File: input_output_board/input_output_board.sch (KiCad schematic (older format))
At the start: 18 parts, among them J1 Neutrik_NCJ6FA-H, J2 Neutrik_NCJ6FA-H, J3 Neutrik_NCJ6FA-H, J4 Neutrik_NCJ6FA-H, J5 AudioJack3, J6 Conn_02x05_Odd_Even, J7 Molex_SL_01x02_Male, J8 Molex_SL_01x02_Male, K1 G6S-2, K2 G6S-2, K3 G6S-2, K4 G6S-2, K5 G6S-2

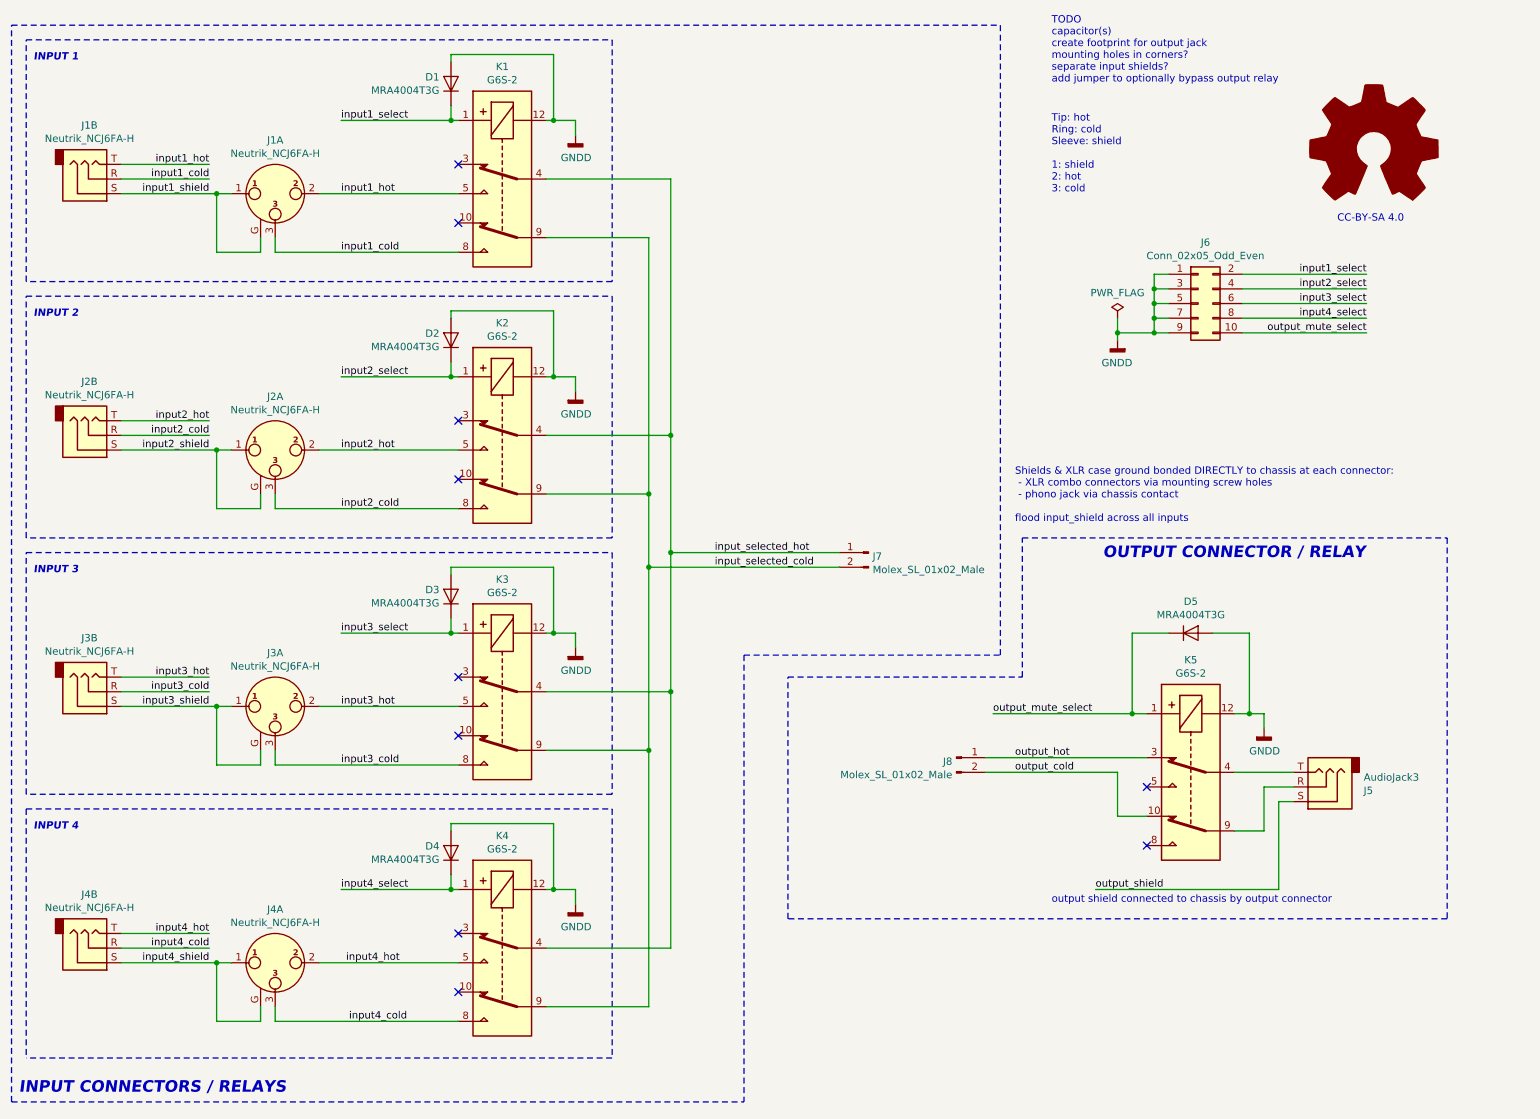
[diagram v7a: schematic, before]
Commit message: add jumpers to schematic to optionally bypass output relay. Update TODO. Clean up schematic
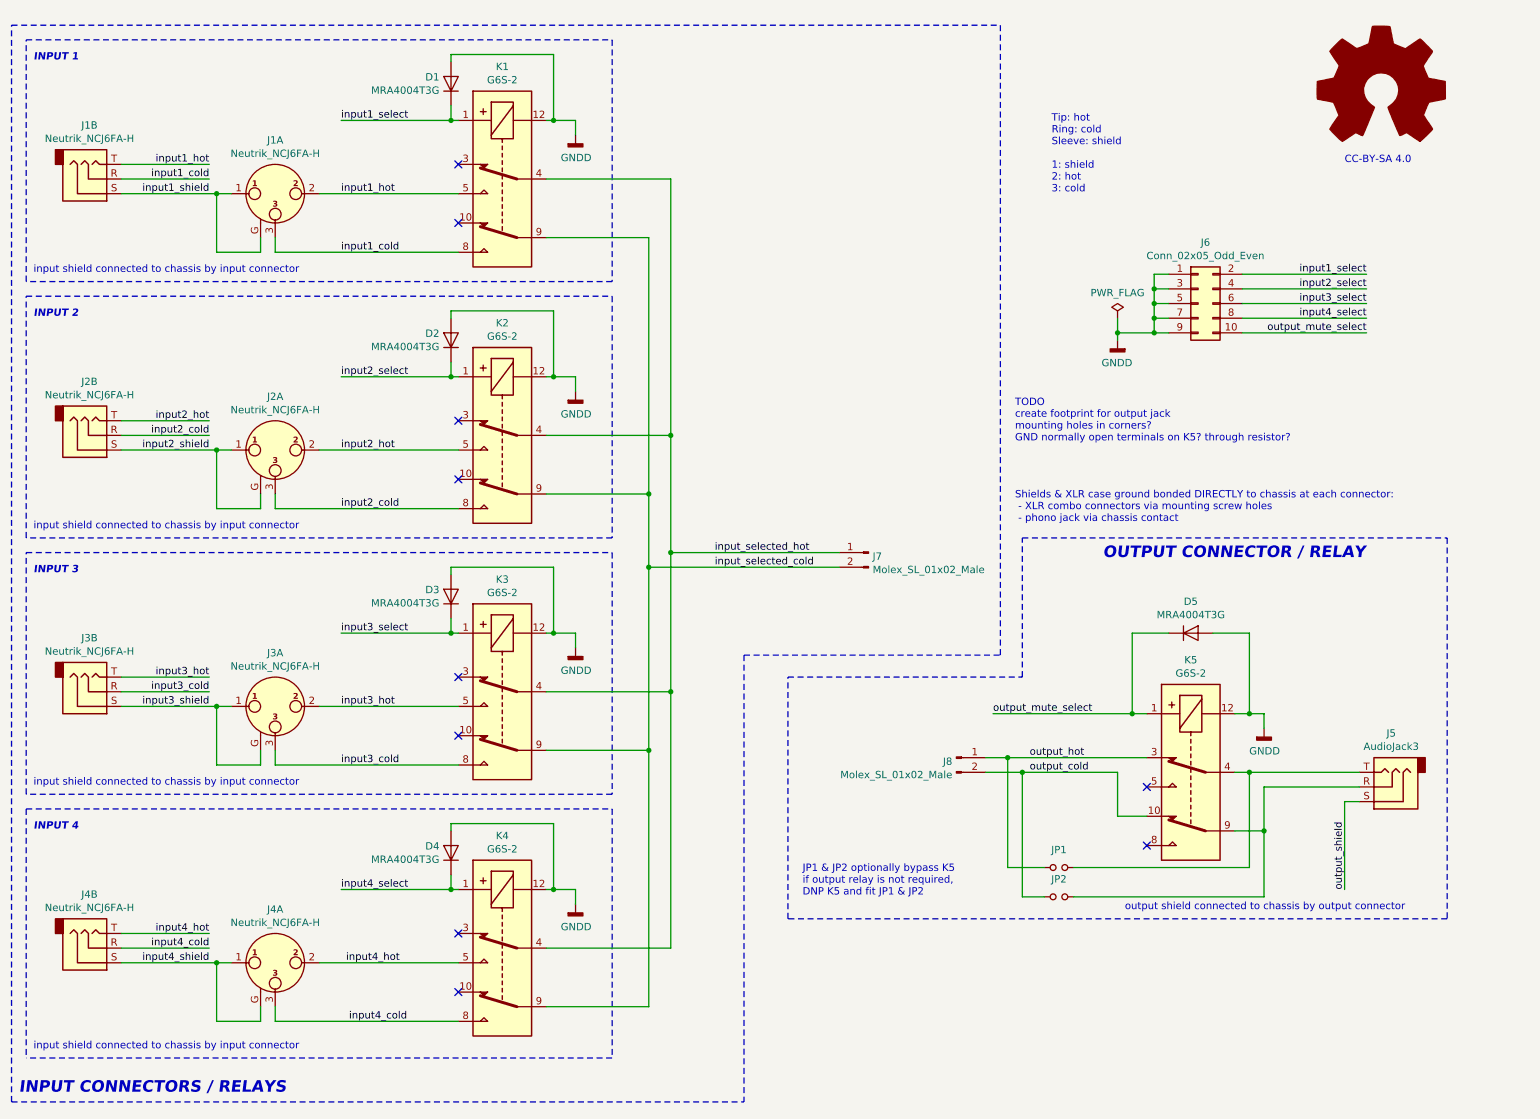
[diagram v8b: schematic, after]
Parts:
- added JP1, JP2: Jumper_NO_Small, Connector_PinHeader_2.54mm:PinHeader_1x02_P2.54mm_Vertical, symbol Device:Jumper_NO_Small
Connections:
- net output_cold: now also JP2.1
- net output_hot: now also JP1.1
- net at J5.R, K5.9: now also JP2.2
- net at J5.T, K5.4: now also JP1.2
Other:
- note added: "JP1 & JP2 optionally bypass K5\nif output relay is not required,\nDNP K5 and fit JP1 & JP2"
- note added: "Shields & XLR case ground bonded DIRECTLY to chassis at each connector:\n - XLR combo connectors via mounting screw holes\n - phono jack via chassis contact"
- note added: "TODO\ncreate footprint for output jack\nmounting holes in corners?\nGND normally open terminals on K5? through resistor?"
- note added: "input shield connected to chassis by input connector"
- note removed: "Shields & XLR case ground bonded DIRECTLY to chassis at each connector:\n - XLR combo connectors via mounting screw holes\n - phono jack via chassis contact\n\nflood input_shield across all inputs"
- note removed: "TODO\ncapacitor(s)\ncreate footprint for output jack\nmounting holes in corners?\nseparate input shields?\nadd jumper to optionally bypass output relay"
- moved on the sheet: J5
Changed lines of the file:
@@
 L Connector:AudioJack3 J5
 U 1 1 5CAA8F23
-P 9600 5750
-F 0 "J5" H 9320 5775 50  0000 R CNN
-F 1 "AudioJack3" H 9320 5684 50  0000 R CNN
-F 2 "Connector_Audio:Jack_3.5mm_Neutrik_NMJ6HCD2_Horizontal" H 9600 5750 50  0001 C CNN
-F 3 "https://www.neutrik.us/media/8560/download/nrj3hf-1-2.pdf?v=1" H 9600 5750 50  0001 C CNN
-F 4 "Neutrik" H 9600 5750 50  0001 C CNN "Manufacturer"
-F 5 "NRJ3HF-1" H 9600 5750 50  0001 C CNN "Manufacturer PN"
-F 6 "Mouser" H 9600 5750 50  0001 C CNN "Distributor"
-F 7 "568-NRJ3HF-1" H 9600 5750 50  0001 C CNN "Distributor PN"
-F 8 "https://www.mouser.com/ProductDetail/568-NRJ3HF-1" H 9600 5750 50  0001 C CNN "URL"
-F 9 "0.63" H 9600 5750 50  0001 C CNN "Unit Price"
-	1    9600 5750
+P 10050 5750
+F 0 "J5" H 10032 5383 50  0000 C CNN
+F 1 "AudioJack3" H 10032 5474 50  0000 C CNN
+F 2 "Connector_Audio:Jack_3.5mm_Neutrik_NMJ6HCD2_Horizontal" H 10050 5750 50  0001 C CNN
+F 3 "https://www.neutrik.us/media/8560/download/nrj3hf-1-2.pdf?v=1" H 10050 5750 50  0001 C CNN
+F 4 "Neutrik" H 10050 5750 50  0001 C CNN "Manufacturer"
+F 5 "NRJ3HF-1" H 10050 5750 50  0001 C CNN "Manufacturer PN"
+F 6 "Mouser" H 10050 5750 50  0001 C CNN "Distributor"
+F 7 "568-NRJ3HF-1" H 10050 5750 50  0001 C CNN "Distributor PN"
+F 8 "https://www.mouser.com/ProductDetail/568-NRJ3HF-1" H 10050 5750 50  0001 C CNN "URL"
+F 9 "0.63" H 10050 5750 50  0001 C CNN "Unit Price"
+	1    10050 5750
 	-1   0    0    1
 $EndComp
@@
 	2150 5200 2050 5200
 Wire Wire Line
-	8200 5650 7300 5650
-Text Label 7500 5550 0    50   ~ 0
+	8200 5650 7550 5650
+Text Label 7600 5550 0    50   ~ 0
 output_hot
-Text Label 7500 5650 0    50   ~ 0
+Text Label 7600 5650 0    50   ~ 0
 output_cold
 Wire Wire Line
@@
 $EndComp
 Wire Wire Line
-	9400 5650 9000 5650
+	9850 5650 9100 5650
 Wire Wire Line
 	9000 6050 9200 6050
@@
 	9200 6050 9200 5750
 Wire Wire Line
-	9200 5750 9400 5750
+	9200 5750 9850 5750
 Wire Wire Line
 	8200 5650 8200 5950
@@
 	8200 5950 8400 5950
 Wire Wire Line
-	7300 5550 8400 5550
-Wire Wire Line
-	8050 6450 9300 6450
-Wire Wire Line
-	9300 6450 9300 5850
-Wire Wire Line
-	9300 5850 9400 5850
+	7300 5550 7450 5550
+Wire Wire Line
+	9750 6450 9750 5850
+Wire Wire Line
+	9750 5850 9850 5850
 Wire Wire Line
 	8550 4700 8300 4700
@@
 Connection ~ 8200 2650
 Text Notes 7500 3950 0    50   ~ 0
-Shields & XLR case ground bonded DIRECTLY to chassis at each connector:\n - XLR combo connectors via mounting screw holes\n - phono jack via chassis contact\n\nflood input_shield across all inputs
+Shields & XLR case ground bonded DIRECTLY to chassis at each connector:\n - XLR combo connectors via mounting screw holes\n - phono jack via chassis contact
 Wire Wire Line
 	2350 2100 2350 2000
@@
 Wire Wire Line
 	2450 2100 3700 2100
-Text Notes 7750 950  0    50   ~ 0
-TODO\ncapacitor(s)\ncreate footprint for output jack\nmounting holes in corners?\nseparate input shields?\nadd jumper to optionally bypass output relay
 Wire Notes Line
 	7550 4050 10450 4050
@@
 Wire Wire Line
 	1400 1700 2050 1700
-Text Label 8050 6450 0    50   ~ 0
+Text Label 9750 6450 1    50   ~ 0
 output_shield
-Text Notes 7750 6550 0    50   ~ 0
+Text Notes 8250 6600 0    50   ~ 0
 output shield connected to chassis by output connector
 $Comp
 L Graphic:Logo_Open_Hardware_Large #LOGO?
 U 1 1 5D0E77C4
-P 9950 1400
-F 0 "#LOGO?" H 9950 1900 50  0001 C CNN
-F 1 "Logo_Open_Hardware_Large" H 9950 1000 50  0001 C CNN
-F 2 "" H 9950 1400 50  0001 C CNN
-F 3 "~" H 9950 1400 50  0001 C CNN
-	1    9950 1400
-	1    0    0    -1
-$EndComp
-Text Notes 9700 1900 0    50   ~ 0
+P 10000 1000
+F 0 "#LOGO?" H 10000 1500 50  0001 C CNN
+F 1 "Logo_Open_Hardware_Large" H 10000 600 50  0001 C CNN
+F 2 "" H 10000 1000 50  0001 C CNN
+F 3 "~" H 10000 1000 50  0001 C CNN
+	1    10000 1000
+	1    0    0    -1
+$EndComp
+Text Notes 9750 1500 0    50   ~ 0
 CC-BY-SA 4.0
+$Comp
+L Device:Jumper_NO_Small JP1
+U 1 1 5D10F46D
+P 7800 6300
+F 0 "JP1" H 7800 6421 50  0000 C CNN
+F 1 "Jumper_NO_Small" H 7800 6421 50  0001 C CNN
+F 2 "Connector_PinHeader_2.54mm:PinHeader_1x02_P2.54mm_Vertical" H 7800 6300 50  0001 C CNN
+F 3 "~" H 7800 6300 50  0001 C CNN
+	1    7800 6300
+	1    0    0    -1
+$EndComp
+Wire Wire Line
+	7450 5550 7450 6300
+Wire Wire Line
+	7450 6300 7700 6300
+Connection ~ 7450 5550
+Wire Wire Line
+	7450 5550 8400 5550
+Wire Wire Line
+	7550 5650 7550 6500
+Wire Wire Line
+	7550 6500 7700 6500
+Connection ~ 7550 5650
+Wire Wire Line
+	7550 5650 7300 5650
+Wire Wire Line
+	7900 6500 9200 6500
+Wire Wire Line
+	9200 6500 9200 6050
+Connection ~ 9200 6050
+Wire Wire Line
+	7900 6300 9100 6300
+Wire Wire Line
+	9100 6300 9100 5650
+Connection ~ 9100 5650
+Wire Wire Line
+	9100 5650 9000 5650
+Text Notes 800  2250 0    50   ~ 0
+input shield connected to chassis by input connector
+Text Notes 800  4000 0    50   ~ 0
+input shield connected to chassis by input connector
+Text Notes 800  5750 0    50   ~ 0
+input shield connected to chassis by input connector
+Text Notes 800  7550 0    50   ~ 0
+input shield connected to chassis by input connector
+Text Notes 7500 3400 0    50   ~ 0
+TODO\ncreate footprint for output jack\nmounting holes in corners?\nGND normally open terminals on K5? through resistor?
+Text Notes 6050 6500 0    50   ~ 0
+JP1 & JP2 optionally bypass K5\nif output relay is not required,\nDNP K5 and fit JP1 & JP2
+$Comp
+L Device:Jumper_NO_Small JP2
+U 1 1 5D17EFC9
+P 7800 6500
+F 0 "JP2" H 7800 6621 50  0000 C CNN
+F 1 "Jumper_NO_Small" H 7800 6621 50  0001 C CNN
+F 2 "Connector_PinHeader_2.54mm:PinHeader_1x02_P2.54mm_Vertical" H 7800 6500 50  0001 C CNN
+F 3 "~" H 7800 6500 50  0001 C CNN
+	1    7800 6500
+	1    0    0    -1
+$EndComp
 $EndSCHEMATC
